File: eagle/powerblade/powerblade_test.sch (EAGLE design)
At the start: 118 parts, among them J1 JTAG_14PIN_IDC-NL, J21 AC_INFILM, Q1 2N7002, U1 TPS62122, U2 TR1000, U3 MSP430FR5738, U4 LTC5800, U5 MAX9910, U6 MAX9910, U7 OPA2369, X1 ABM8G, X2 ABS07, Y1 UREACH_XTEND, Y2 ANT-916

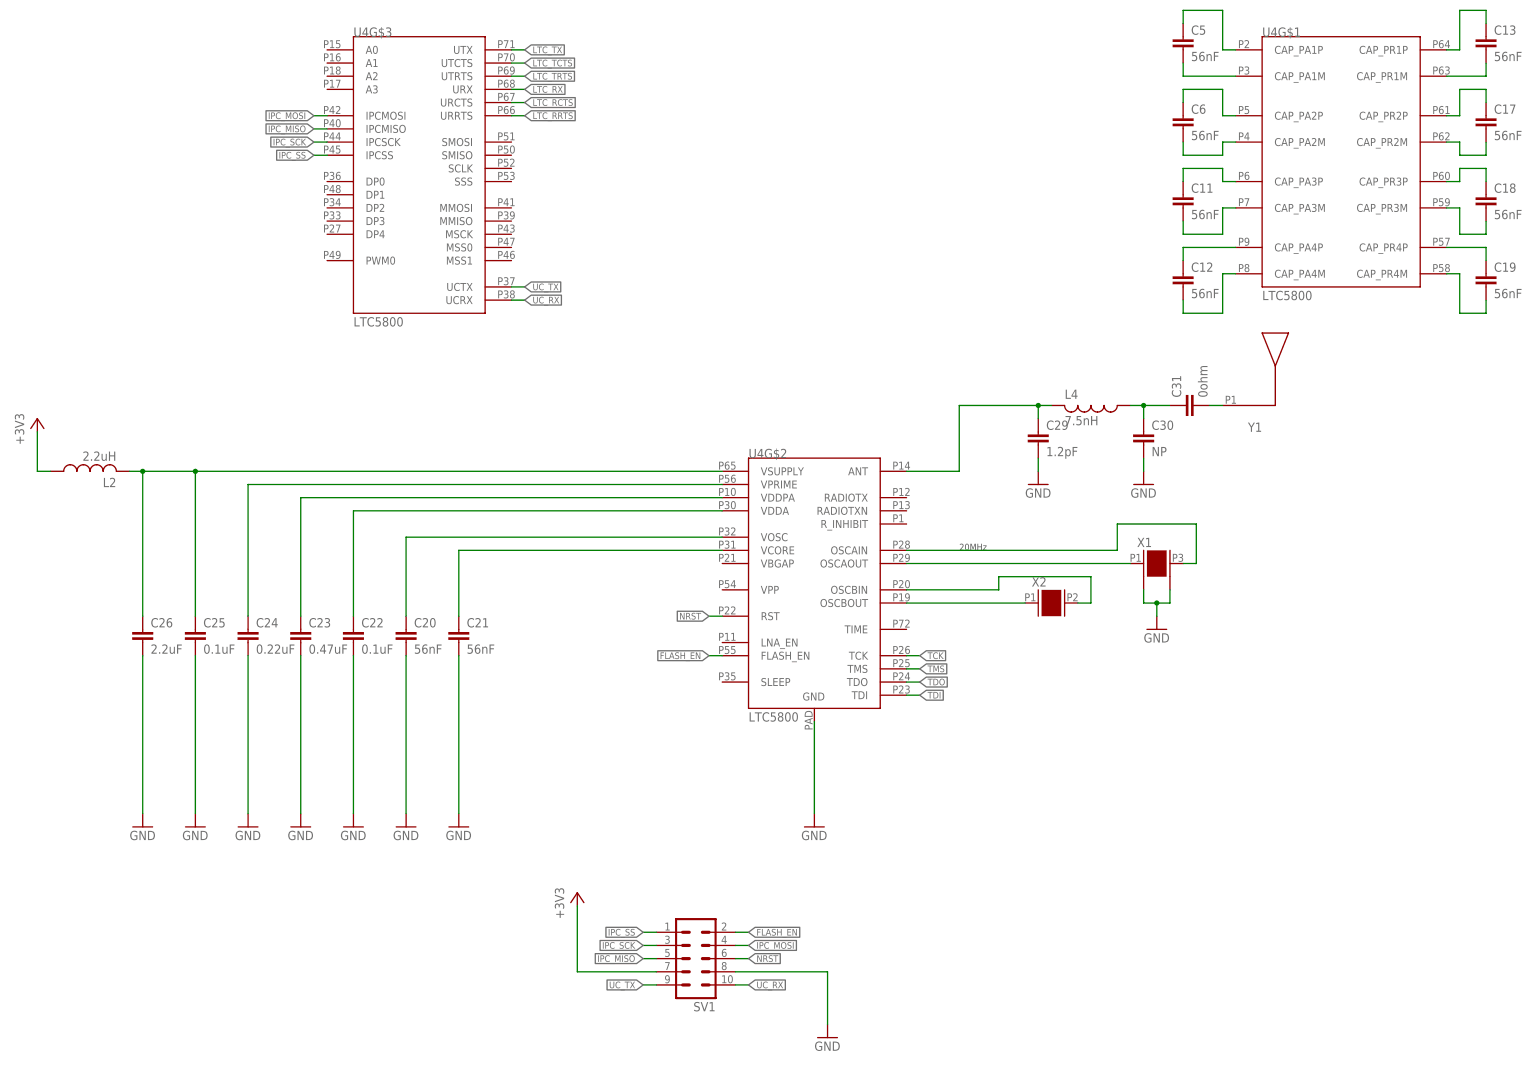
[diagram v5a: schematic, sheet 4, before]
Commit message: added power gating or turnoff ability to tr1000, ltc5800, and power metering and defaulted to off
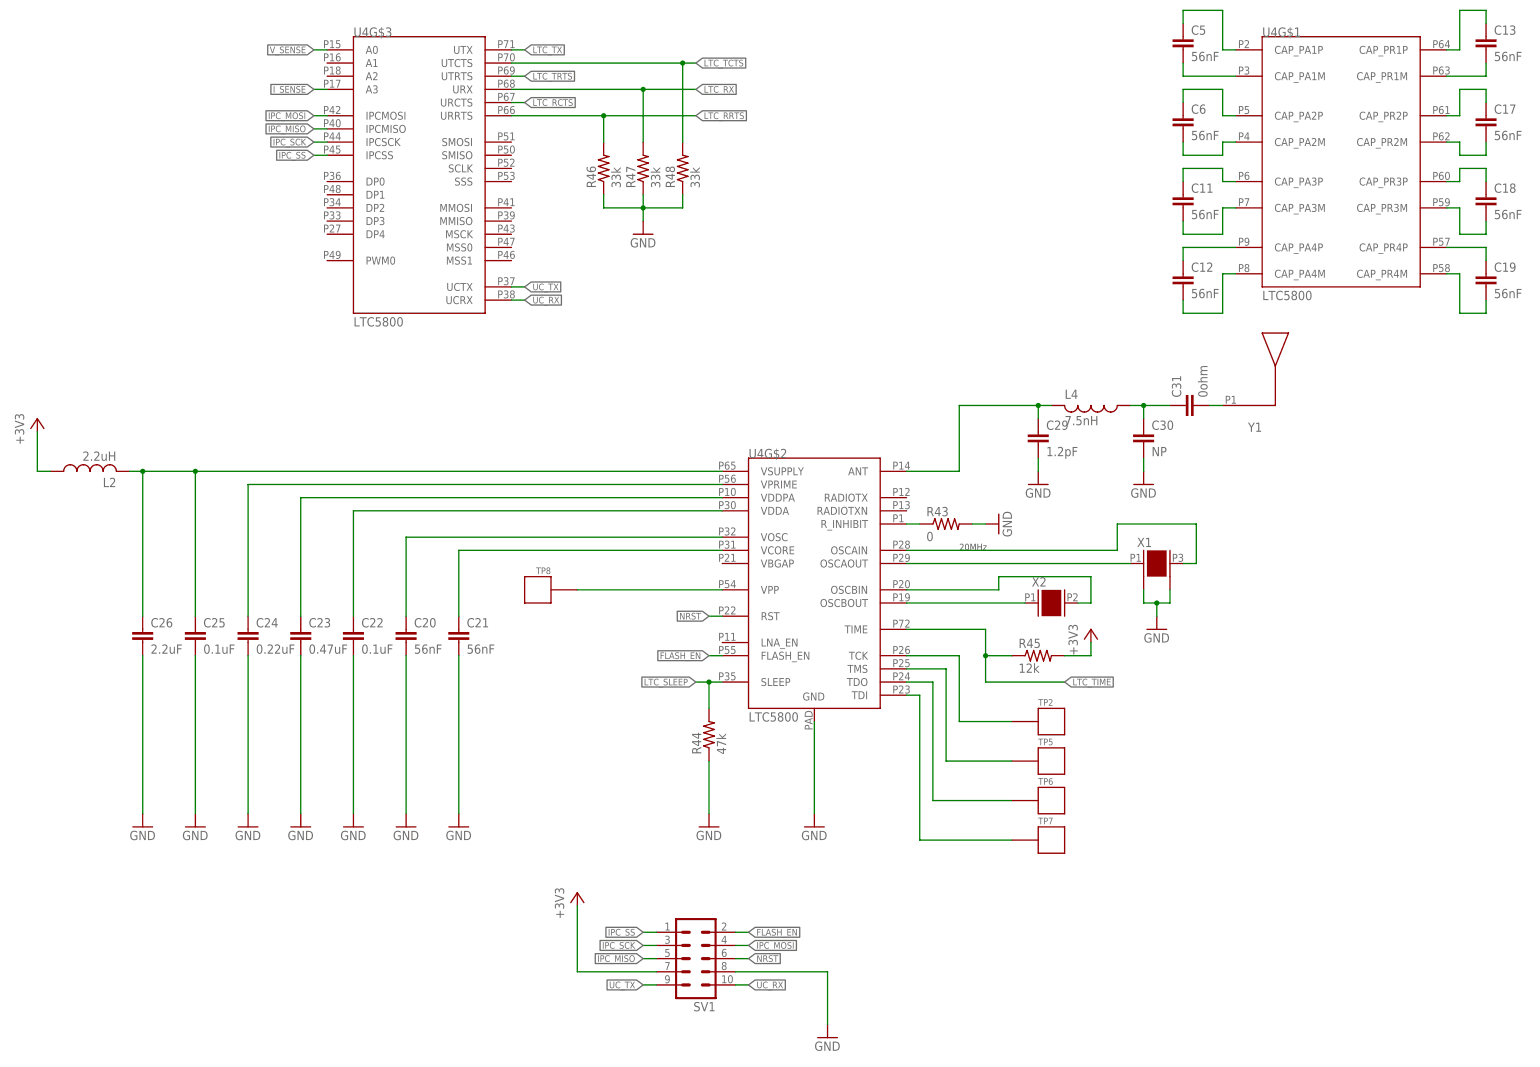
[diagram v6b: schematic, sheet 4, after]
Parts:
- removed Q1: 2N7002, nav:2N7002
- removed R10: 10k, rcl:R-US_R0402
- removed R11: 47k, rcl:R-US_R0603
- removed TP1: TP_STD, skyspecs:TP_STD
- added Q2: 2N7002, nav:2N7002
- added R43: 0, rcl:R-US_R0603
- added R44, R49: 47k, rcl:R-US_R0603
- added R45: 12k, rcl:R-US_R0603
- added R46, R47, R48: 33k, rcl:R-US_R0603
- added TP2, TP5, TP6, TP7, TP8: TP_STD, skyspecs:TP_STD
- R13: value 10 -> 1 1%
- R15: value 1M 0.1% -> NP; DIGIKEY A102234CT-ND -> NP
- R16: value 15 0.1% -> 0; DIGIKEY A109933CT-ND -> (none)
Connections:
- removed net N$16: Q1.D, R10.1, U1.EN
- removed net N$61: R34.1, U3.P2.1/TB0.0/UCARX/MISO
- removed net PS_!EN!: Q1.G, R11.1, TP1.P$1
- new net DGND: C27.2, C28.2, C38.2, Q2.D, R16.1, R18.1, R21.1, R38.1, R39.PW, RI2.1, U5.VSS, U6.VSS, U7G$1.VSS
- new net LTC_SLEEP: R44.2, U3.P2.2/UCBCLK, U4G$2.SLEEP
- new net LTC_TIME: R45.1, U4G$2.TIME
- new net METER_EN: Q2.G, R49.2, U3.P1.7/TA1.0/UCBSCL/MISO
- new net N$72: TP7.P$1, U4G$2.TDI
- new net N$73: TP6.P$1, U4G$2.TDO
- new net N$74: TP5.P$1, U4G$2.TMS
- new net N$75: TP2.P$1, U4G$2.TCK
- new net N$76: R43.1, U4G$2.R_INHIBIT
- net +3V3: now also R45.2
- net GND: now also Q2.S, R43.2, R44.1, R46.1, R47.1, R48.1, R49.1; no longer C27.2, C28.2, C38.2, Q1.S, R11.2, R16.1, R18.1, R21.1, R38.1, R39.PW, RI2.1, U5.VSS, U6.VSS, U7G$1.VSS
- net I_SENSE: now also U3.P1.5/TB0.2/UCACLK, U4G$3.A3
- net LTC_RRTS: now also R46.2
- net LTC_RX: now also R33.1, R47.2, U3.P2.0/UCATX/MOSI
- net LTC_TCTS: now also R48.2
- net LTC_TX: now also R34.1, U3.P2.1/TB0.0/UCARX/MISO
- net N$60: now also TP8.P$1, U4G$2.VPP; no longer R33.1, U3.P2.0/UCATX/MOSI
- net TCK: no longer U4G$2.TCK
- net TDI: no longer U4G$2.TDI
- net TDO: no longer U4G$2.TDO
- net TMS: no longer U4G$2.TMS
- net VCC: now also U1.EN; no longer R10.2
- net V_SENSE: now also U3.P1.4/TB0.1/A4, U4G$3.A0
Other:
- moved on the sheet: R33, R34

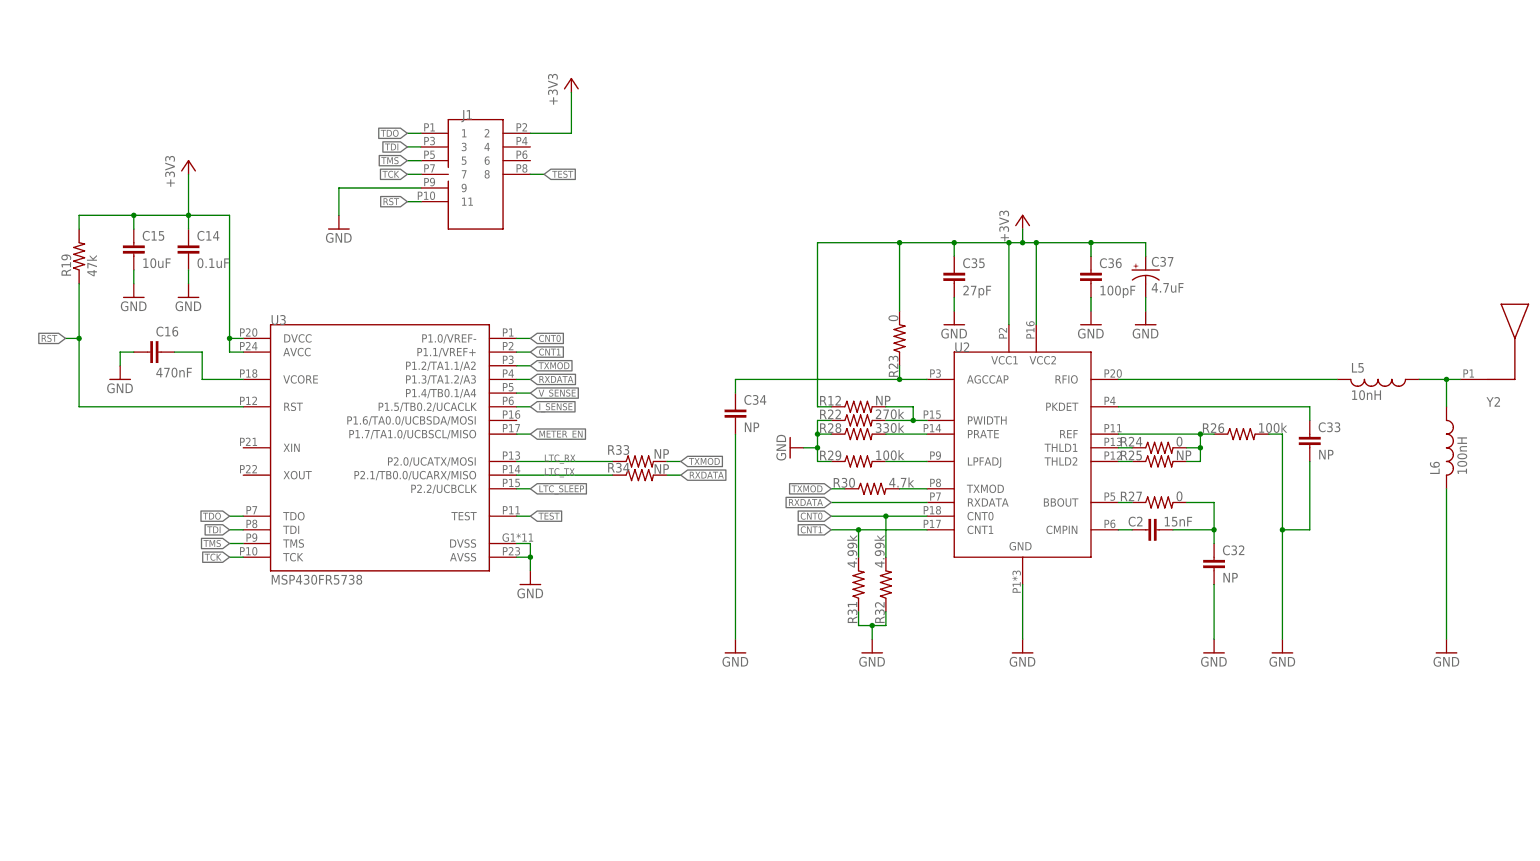
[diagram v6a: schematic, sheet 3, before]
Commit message: finished layout incl antennas
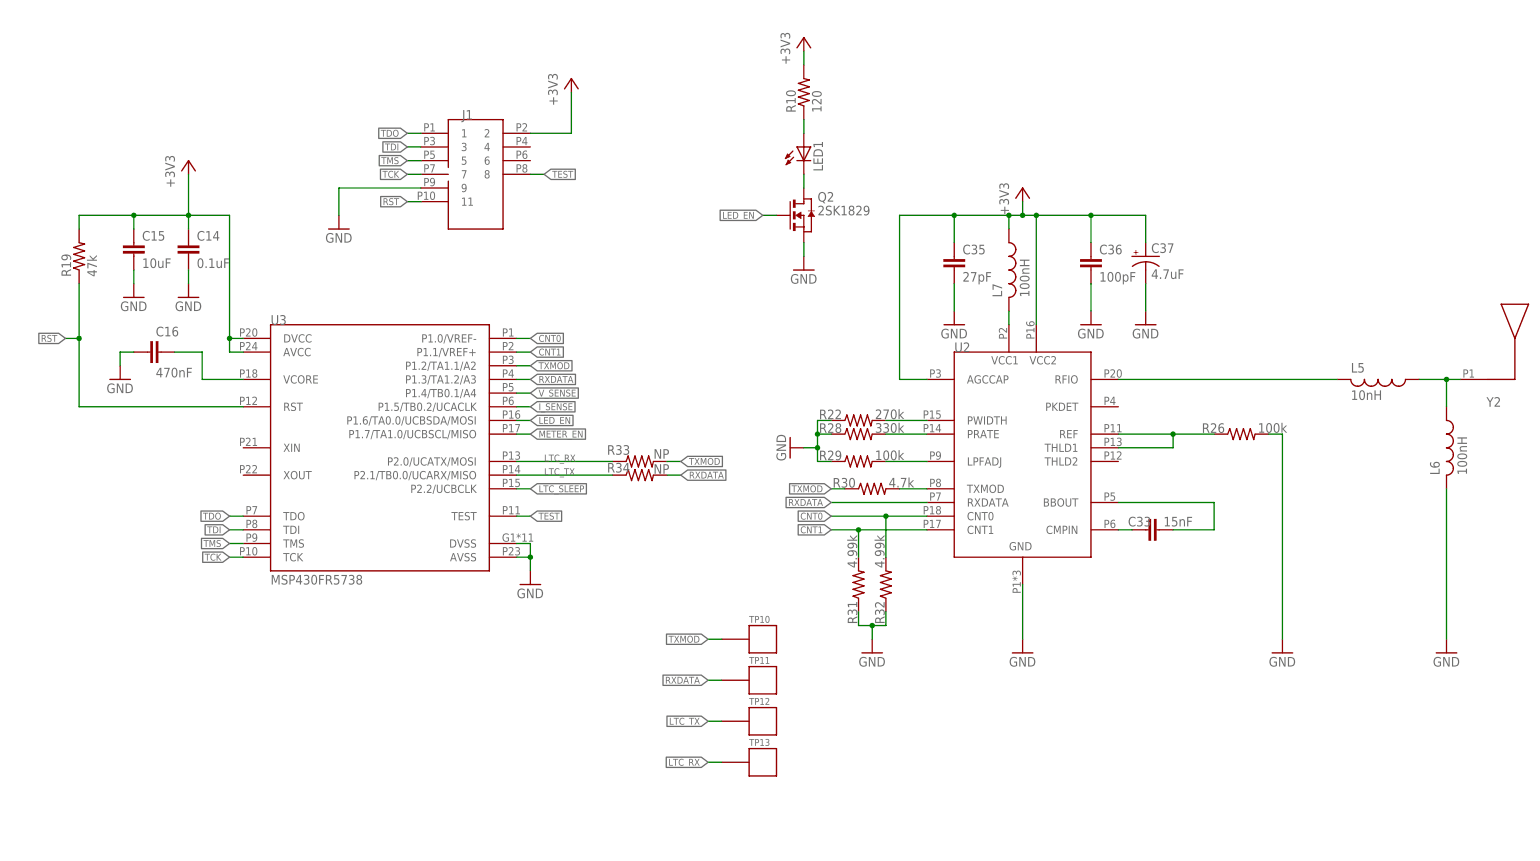
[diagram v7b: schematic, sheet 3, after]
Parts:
- removed C34: NP, rcl:C-EUC0603
- removed C8: 0.1uF, rcl:C-EUC0402
- removed R12, R25: NP, rcl:R-US_R0603
- removed R23, R24, R27: 0, rcl:R-US_R0603
- removed RS-, VS+, VS-: TP_STD, skyspecs:TP_STD
- added ACSLOT: AC_NODIM, powerfilm:AC_NODIM
- added L7: 100nH, rcl:L-USL0603
- added LED1: (no value), SparkFun-LED:LED0603
- added Q1: 2SK1829, powerfilm:2SK1829
- added R10: 120, rcl:R-US_R0603
- added TP1, TP9, TPGND1, TPGND2: TP_MULT, skyspecs:TP_MULT
- added TP10, TP11, TP12, TP13: TP_STD, skyspecs:TP_STD
- C10: device rcl:C-EUC0603 -> rcl:C-EUC0402; DIGIKEY 587-2786-1-ND -> 490-5915-1-ND
- C2: value 15nF -> NP; device rcl:C-EUC0603 -> rcl:C-EUC2220K; DIGIKEY (none) -> NP
- C29, C30, C31: device rcl:C-EUC0201 -> rcl:C-EUC0402
- C32: value NP -> 33uF; DIGIKEY (none) -> 718-1672-1-ND
- C33: value NP -> 15nF
- C39: device rcl:C-EUC0603 -> rcl:C-EUC0402
- C4: device rcl:C-EUC0603 -> rcl:C-EUC0402; DIGIKEY 399-1053-1-ND -> (none)
- C7: device rcl:C-EUC0402 -> rcl:C-EUC0603; DIGIKEY 587-2786-1-ND -> 490-5915-1-ND
- CS+, CS-, HVS, RS+, TP3, TP4: value TP_STD -> TP_MULT; device skyspecs:TP_STD -> skyspecs:TP_MULT
- J21: value AC_INFILM -> AC_INSW; device powerfilm:AC_INFILM -> powerfilm:AC_INSW; DIGIKEY NP -> (none)
- L4: device rcl:L-USL0201 -> rcl:L-USL0402
- Q2: value 2N7002 -> 2SK1829; device nav:2N7002 -> powerfilm:2SK1829
- R14: device rcl:R-US_R0603 -> rcl:R-US_R0402; DIGIKEY P200HCT-ND -> (none)
- R15, R16, R35, R37, R38, R40, R43, R44, R45, R46, R47, R48: device rcl:R-US_R0603 -> rcl:R-US_R0402
- R17: device rcl:R-US_R0603 -> rcl:R-US_R0402; DIGIKEY A102234CT-ND -> (none)
- R18: device rcl:R-US_R0603 -> rcl:R-US_R0402; DIGIKEY P49.9HCT-ND -> (none)
- R20, R21, RF: device rcl:R-US_R0603 -> rcl:R-US_R0402; DIGIKEY P1.00KHCT-ND -> (none)
- R7: device rcl:R-US_R0603 -> rcl:R-US_R0402; DIGIKEY P560KHCT-ND -> (none)
- R9: device rcl:R-US_R0603 -> rcl:R-US_R0402; DIGIKEY P180KHCT-ND -> (none)
- RI1, RI2: device rcl:R-US_R0603 -> rcl:R-US_R0402; DIGIKEY P120KHCT-ND -> (none)
- TP2, TP5, TP6, TP7: value TP_STD -> TP_SMD; device skyspecs:TP_STD -> skyspecs:TP_SMD
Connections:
- removed net N$1: C1.2, HVS.P$1, R1.2, R8.1
- removed net N$56: R24.2, R25.2, R26.1, U2.REF
- removed net N$58: R25.1, U2.THLD2
- removed net N$59: C33.1, U2.PKDET
- new net LED_EN: Q2.G, U3.P1.6/TA0.0/UCBSDA/MOSI
- new net N$16: L7.2, U2.VCC1
- net +3V3: now also L7.1, R10.2, U2.AGCCAP; no longer R12.1, R23.2, U2.VCC1, VS+.P$1
- net DGND: now also Q1.D; no longer Q2.D
- net GND: now also Q1.S, TPGND1.P$1, TPGND2.P$1; no longer C33.2, C34.2, C8.2, RS-.P$1, VS-.P$1
- net LTC_RX: now also TP13.P$1
- net LTC_TX: now also TP12.P$1
- net METER_EN: now also Q1.G; no longer Q2.G
- net N$12: now also C33.2; no longer R27.1
- net N$4: now also C2.1
- net N$49: now also LED1.A, R10.1; no longer C34.1, R23.1, U2.AGCCAP
- net N$50: no longer R12.2
- net N$54: now also LED1.C, Q2.D; no longer C2.2, C32.1, R27.2
- net N$55: now also C33.1; no longer C2.1
- net N$57: now also R26.1, U2.REF; no longer R24.1
- net N$64: now also TP1.P$1
- net N$67: now also TP9.P$1
- net RXDATA: now also TP11.P$1
- net TXMOD: now also TP10.P$1
- net VCC: now also C32.1; no longer C8.1
- net VTEST: now also C1.2, C2.2, HVS.P$1, R1.2, R8.1
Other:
- moved on the sheet: C33, C35, C36, C37, C7, CS+, CS-

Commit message: finished powerblade
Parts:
- added C34, C8: 8pF, rcl:C-EUC0603
- added LED2: (no value), SparkFun-LED:LED0603
- added Q3: 2SK1829, powerfilm:2SK1829
- added R11: 134k 1%, rcl:R-US_R0603
- added R12: 67k 1%, rcl:R-US_R0603
- added R23: 120, rcl:R-US_R0603
- added TP14: TP_STD, skyspecs:TP_STD
- added X3: 32.768kHz, general:CRYSTAL_0805
- J1: value JTAG_14PIN_IDC-NL -> JTAG_14PIN_IDC; device ibat:JTAG_14PIN_IDC-NL -> ibat:JTAG_14PIN_IDC; TAG-CONNECT TC2050-IDC-NL-430 -> (none)
- R38: device rcl:R-US_R0402 -> rcl:R-US_R0603
- TP8: DIGIKEY (none) -> NP
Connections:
- net N$2 renamed N
- net N$6 renamed P
- removed net LED_EN: Q2.G, U3.P1.6/TA0.0/UCBSDA/MOSI
- new net N$1: C34.2, U3.XOUT, X3.P1
- new net N$56: C8.2, U3.XIN, X3.P2
- new net N$58: LED2.A, R23.1
- new net N$59: LED2.C, Q3.D
- new net VCC_SENSE: R11.1, R12.2, U3.P1.3/TA1.2/A3
- net +3V3: now also R23.2
- net GND: now also C34.1, C8.1, Q3.S, R12.1, TP14.P$1
- net I_SENSE: now also U4G$3.A2; no longer U4G$3.A3
- net RXDATA: now also U3.P1.6/TA0.0/UCBSDA/MOSI; no longer U3.P1.3/TA1.2/A3
- net TCK: now also Q2.G
- net TDI: now also Q3.G
- net VCC: now also R11.2
- net V_SENSE: now also U4G$3.A3; no longer U4G$3.A0
